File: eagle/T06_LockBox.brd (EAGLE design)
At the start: 75.2 x 65.8 mm, 29 parts, among them T1 2N3904, T2 2N3904, T3 2N3904

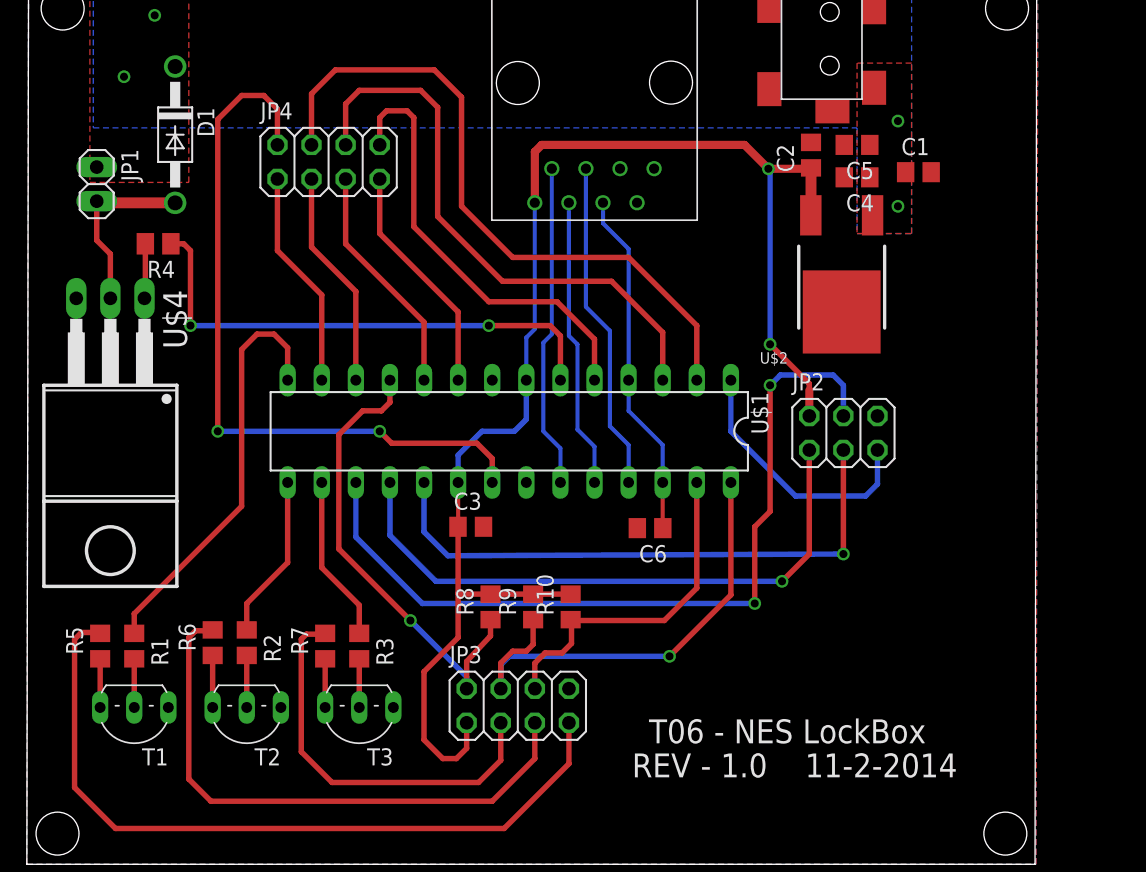
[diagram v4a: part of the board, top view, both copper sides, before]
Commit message: Replaced 10uF 25V 0805 cap with 1206 cap.  0805 package size with those values is not available.
Moved the tplace labels of all components on the .brd
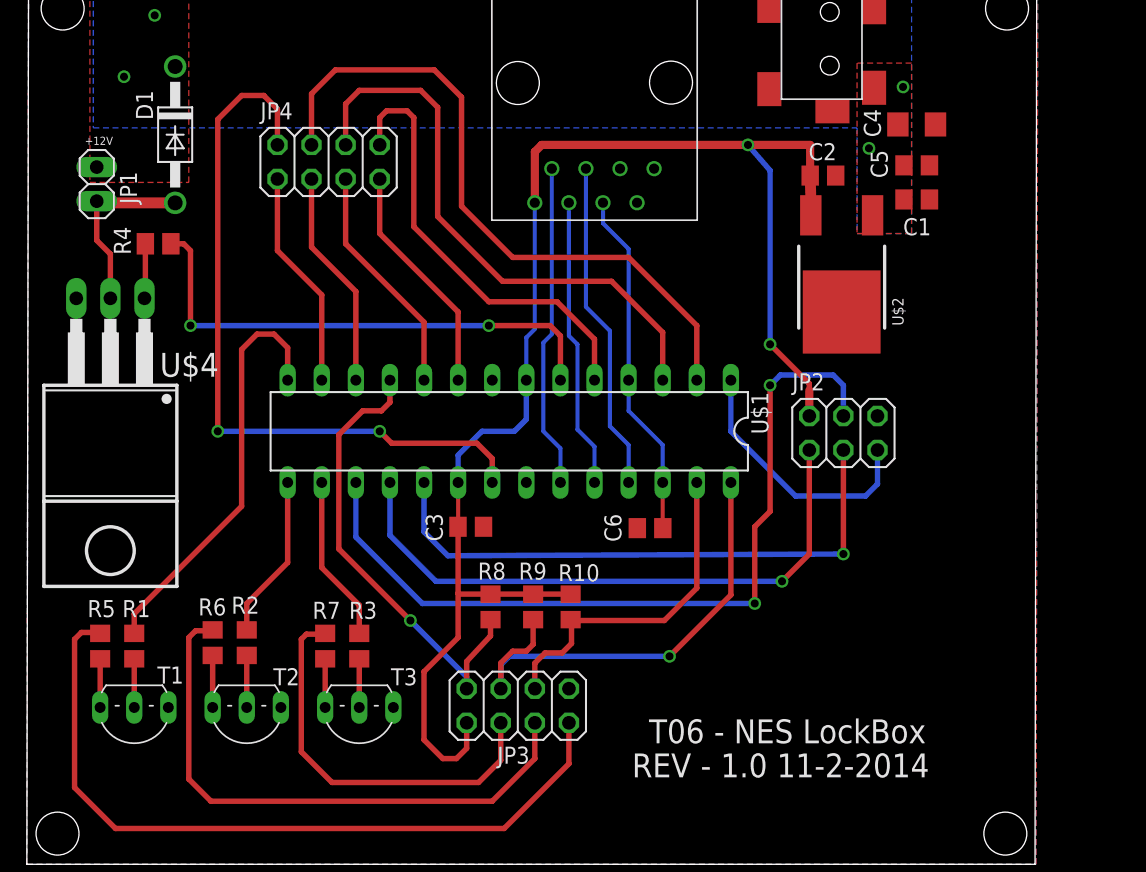
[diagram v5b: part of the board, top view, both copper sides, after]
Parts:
- C1: value 330pF, 24V -> 330pF
- C2: value 10uF, 7V -> 10uF
- C4: device T06_Lockbox:C0805 -> T06_Lockbox:C1206
- moved C4 5.94 mm to (66.3, 55.1), turned to 0 degrees
- moved C5 4.70 mm to (66.3, 52.1), turned to 0 degrees
- moved C1 2.04 mm to (66.3, 49.5)
- moved C2 1.76 mm to (59.3, 51.3), turned to 0 degrees
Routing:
- net 3.3V: track 107.8 -> 111.0 mm
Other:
- board text added: "+12V"

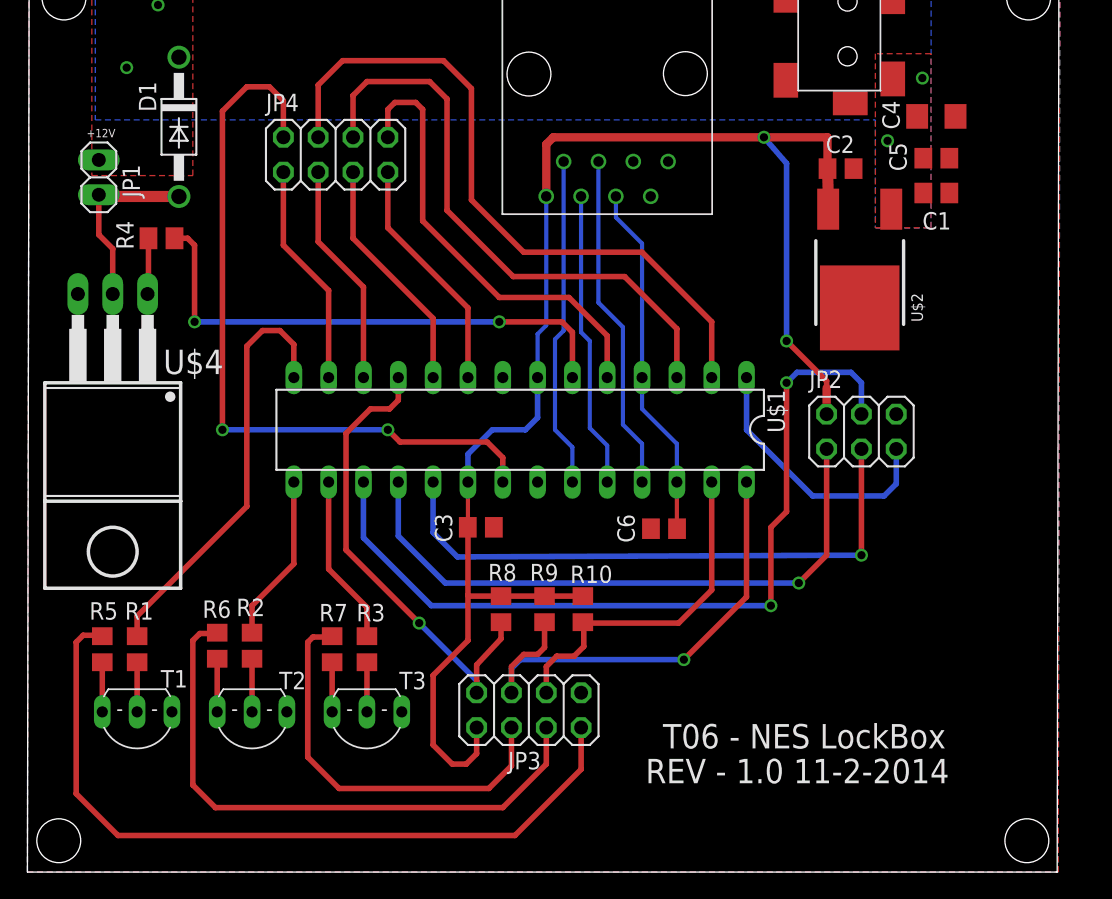
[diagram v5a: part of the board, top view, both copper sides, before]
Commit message: Added 2x5 pin headder and pull up resistor to the ATMEGA reset line.
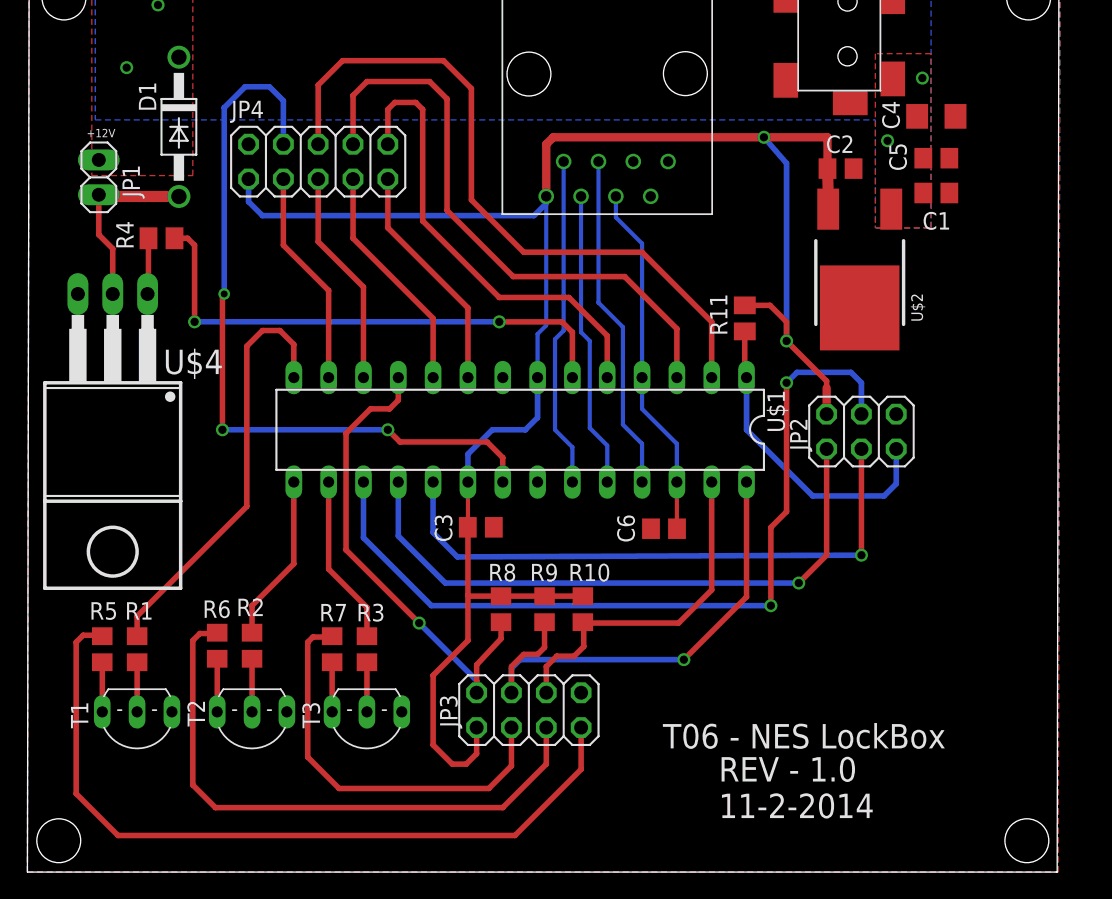
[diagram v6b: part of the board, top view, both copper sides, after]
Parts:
- added R11: 10k, T06_Lockbox:M0805
- JP4: device T06_Lockbox:2X04 -> T06_Lockbox:2X05
- moved JP4 1.37 mm to (21.2, 51.8)
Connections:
- net !RST: now also R11.1
- net 3.3V: now also JP4.1, R11.2
- net AREF: now also JP4.4; no longer JP4.2
- net GND: now also JP4.2
- net PB6: now also JP4.9; no longer JP4.7
- net PB7: now also JP4.7; no longer JP4.5
- net PD0: now also JP4.6; no longer JP4.4
- net PD1: now also JP4.8; no longer JP4.6
- net PD3: now also JP4.10; no longer JP4.8
- net PD6: now also JP4.5; no longer JP4.3
- net PD7: now also JP4.3; no longer JP4.1
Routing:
- net 3.3V: track 111.0 -> 140.1 mm
- net !RST: track 19.6 -> 23.1 mm
- net AREF: track 54.6 -> 55.2 mm, vias 2 -> 3
- net PD7: track 16.4 -> 15.8 mm
- net PD6: track 16.4 -> 15.8 mm
- net PD3: track 33.1 -> 33.6 mm
- net PD1: track 42.9 -> 43.4 mm
- net PD0: track 50.0 -> 50.5 mm
- net PB7: track 17.4 -> 16.9 mm
- net PB6: track 17.4 -> 16.9 mm

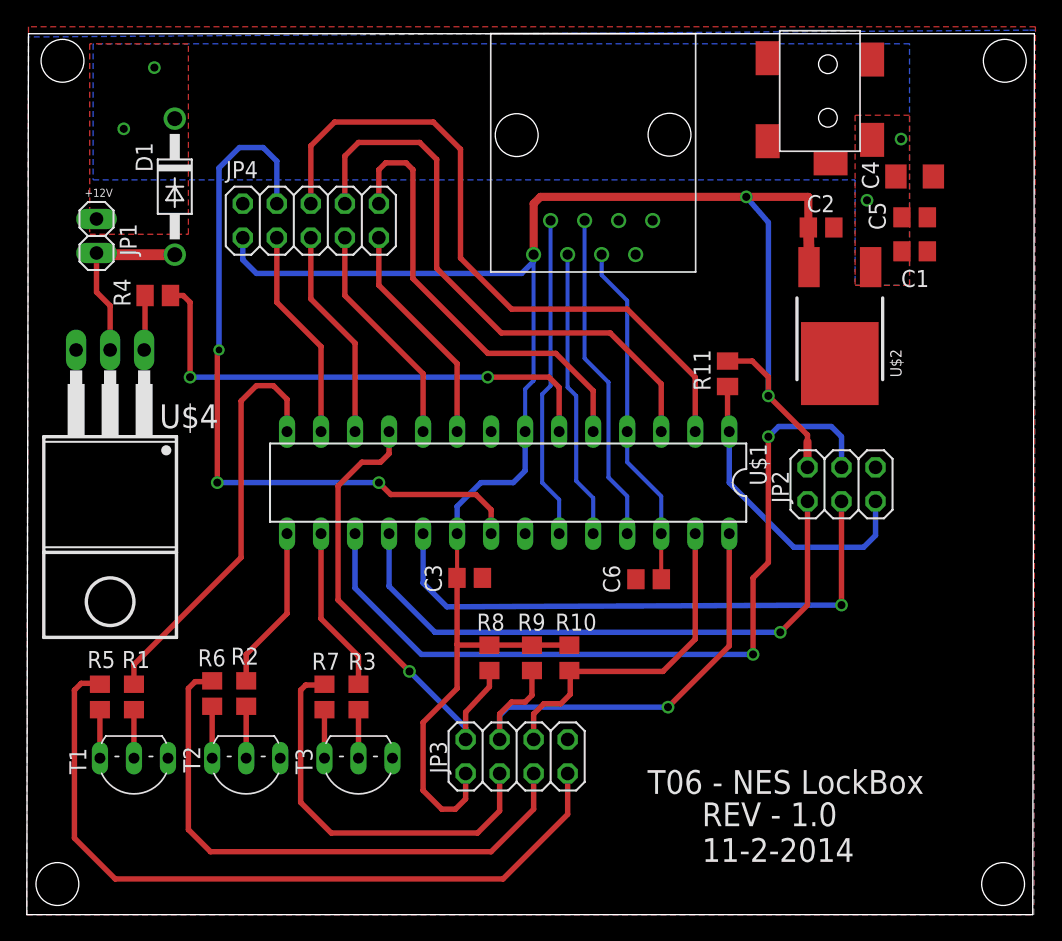
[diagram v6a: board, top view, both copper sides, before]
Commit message: Increased drill size from .76mm to .9mm on the ethernet jack, this should provide enough space for pin diameter variations.
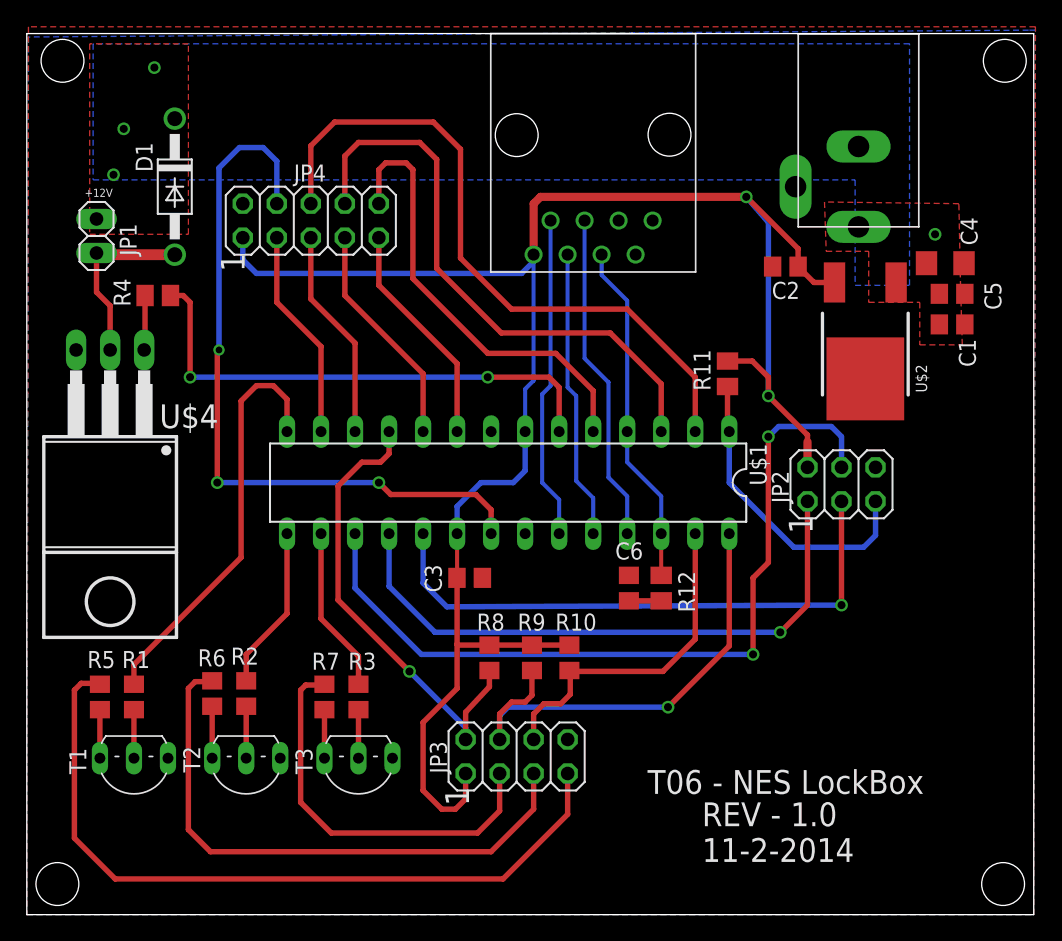
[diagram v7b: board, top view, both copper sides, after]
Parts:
- added R12: (no value), T06_Lockbox:M0805
- U$3: value PJ_075DH -> PJ-102A; device T06_Lockbox:PWR_JACK -> T06_Lockbox:PJ-102A
- moved U$3 9.43 mm to (62.1, 54.4), turned to 0 degrees
- moved C4 6.87 mm to (68.6, 48.6)
- moved C5 6.36 mm to (69.1, 46.4)
- moved C1 6.13 mm to (69.1, 44.1)
- moved C2 3.96 mm to (56.6, 48.4), turned to 180 degrees
- moved U$2 2.22 mm to (62.6, 40.0)
- moved C6 1.61 mm to (45.0, 24.4), turned to 90 degrees
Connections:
- removed net +12V: C1.1, C4.1, C5.1, D1.C, JP1.1, U$2.1, U$3.1
- new net MVOE: C1.1, C4.1, C5.1, D1.C, JP1.1, U$2.1, U$3.P1
- new net N$3: C6.1, R12.2
- net GND: now also U$3.P2, U$3.P3; no longer U$3.2, U$3.3, U$3.P$1, U$3.P$5
- net START: now also R12.1; no longer C6.1
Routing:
- net N$3: track 0.00 -> 2.41 mm
- added copper zone on layer 1, net MVOE
- added copper zone on layer 16, net MVOE
- removed copper zone on layer 1, net +12V
- removed copper zone on layer 16, net +12V
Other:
- outline, holes or cut-outs redrawn
- board text added: "1"

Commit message: Added cap to VCC next to atmel chip, increased 3.3V trace width, text size issue was not related to our file but Andrews eagle that always displayed vector font
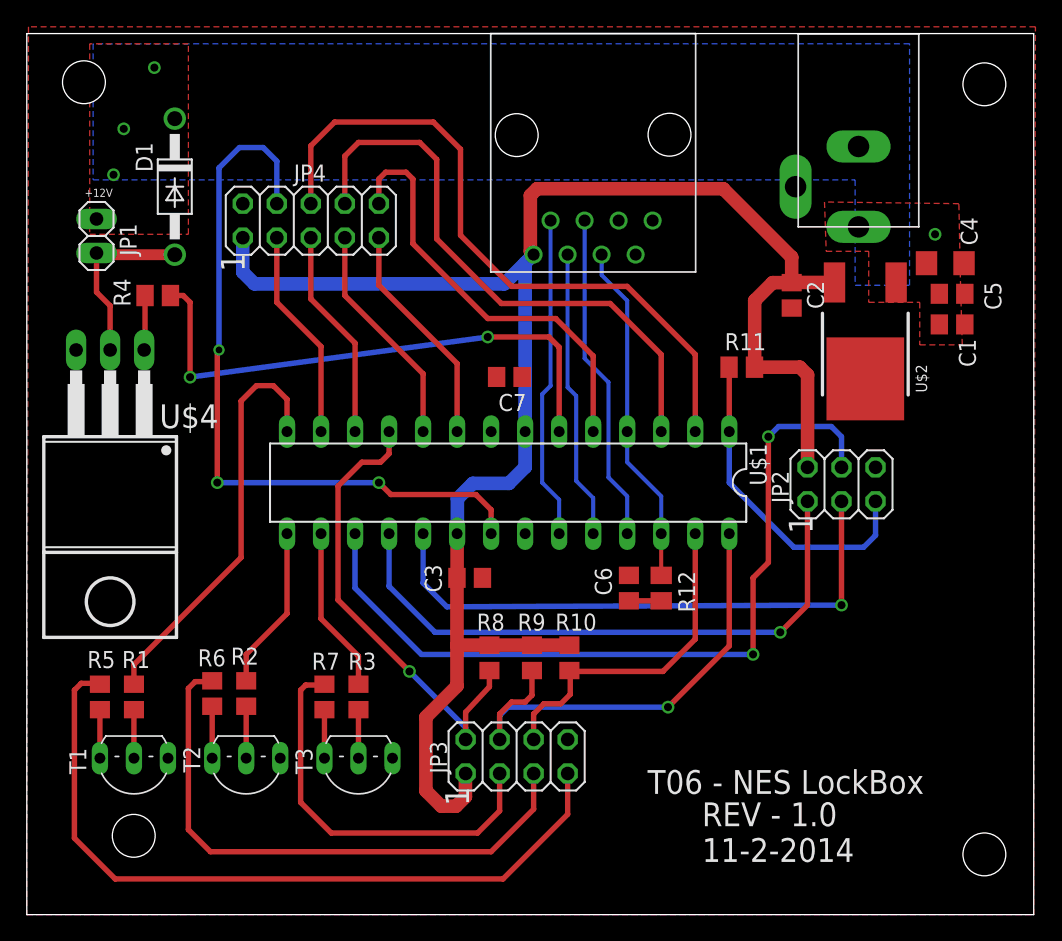
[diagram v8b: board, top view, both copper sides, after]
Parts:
- added C7: 1uF, T06_Lockbox:C0805
- moved C2 2.20 mm to (57.1, 46.2), turned to 270 degrees
- moved R11 1.17 mm to (53.4, 40.9), turned to 0 degrees
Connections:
- net MVOE renamed +12V
- net 3.3V: now also C7.1
- net GND: now also C7.2
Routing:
- net 3.3V: track 140.3 -> 134.6 mm, vias 2 -> 0
- net SOL_EN: track 38.4 -> 41.6 mm
- net PD3: track 33.6 -> 32.2 mm
- net !RST: track 23.1 -> 24.5 mm
- removed copper zone on layer 16, net N$2
